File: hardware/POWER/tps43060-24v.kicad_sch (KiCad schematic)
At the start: 18 parts, among them Q1 CSD17313Q2, Q2 CSD17313Q2, U3 TPS43060RTE

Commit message: 硬件版本v2，待验证
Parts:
- C3, C5: footprint Resistor_SMD:R_0402_1005Metric -> Capacitor_SMD:C_0402_1005Metric
- C4, C6, C7, C8: footprint Capacitor_SMD:C_0805_2012Metric -> Capacitor_SMD:C_0603_1608Metric
- R7: value 76.8K -> 78.7K
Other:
- note added: "F=730K"
- note removed: "F=748K"
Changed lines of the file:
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@@
 		)
 	)
-	(text "F=748K"
+	(text "F=730K"
 		(exclude_from_sim no)
 		(at 104.902 125.73 0)
@@
 			)
 		)
-		(property "Footprint" "Resistor_SMD:R_0402_1005Metric"
+		(property "Footprint" "Capacitor_SMD:C_0402_1005Metric"
 			(at 153.3652 107.95 0)
 			(effects
@@
 			)
 		)
-		(property "Footprint" "Resistor_SMD:R_0402_1005Metric"
+		(property "Footprint" "Capacitor_SMD:C_0402_1005Metric"
 			(at 153.3652 85.09 0)
 			(effects
@@
 			)
 		)
-		(property "Footprint" "Capacitor_SMD:C_0805_2012Metric"
+		(property "Footprint" "Capacitor_SMD:C_0603_1608Metric"
 			(at 61.9252 101.6 0)
 			(effects
@@
 			)
 		)
-		(property "Footprint" "Capacitor_SMD:C_0805_2012Metric"
+		(property "Footprint" "Capacitor_SMD:C_0603_1608Metric"
 			(at 228.2952 110.49 0)
 			(effects
@@
 			)
 		)
-		(property "Footprint" "Capacitor_SMD:C_0805_2012Metric"
+		(property "Footprint" "Capacitor_SMD:C_0603_1608Metric"
 			(at 210.5152 110.49 0)
 			(effects
@@
 			)
 		)
-		(property "Value" "76.8K"
+		(property "Value" "78.7K"
 			(at 101.6 121.9199 0)
 			(effects
@@
 			)
 		)
-		(property "Footprint" "Capacitor_SMD:C_0805_2012Metric"
+		(property "Footprint" "Capacitor_SMD:C_0603_1608Metric"
 			(at 219.4052 110.49 0)
 			(effects

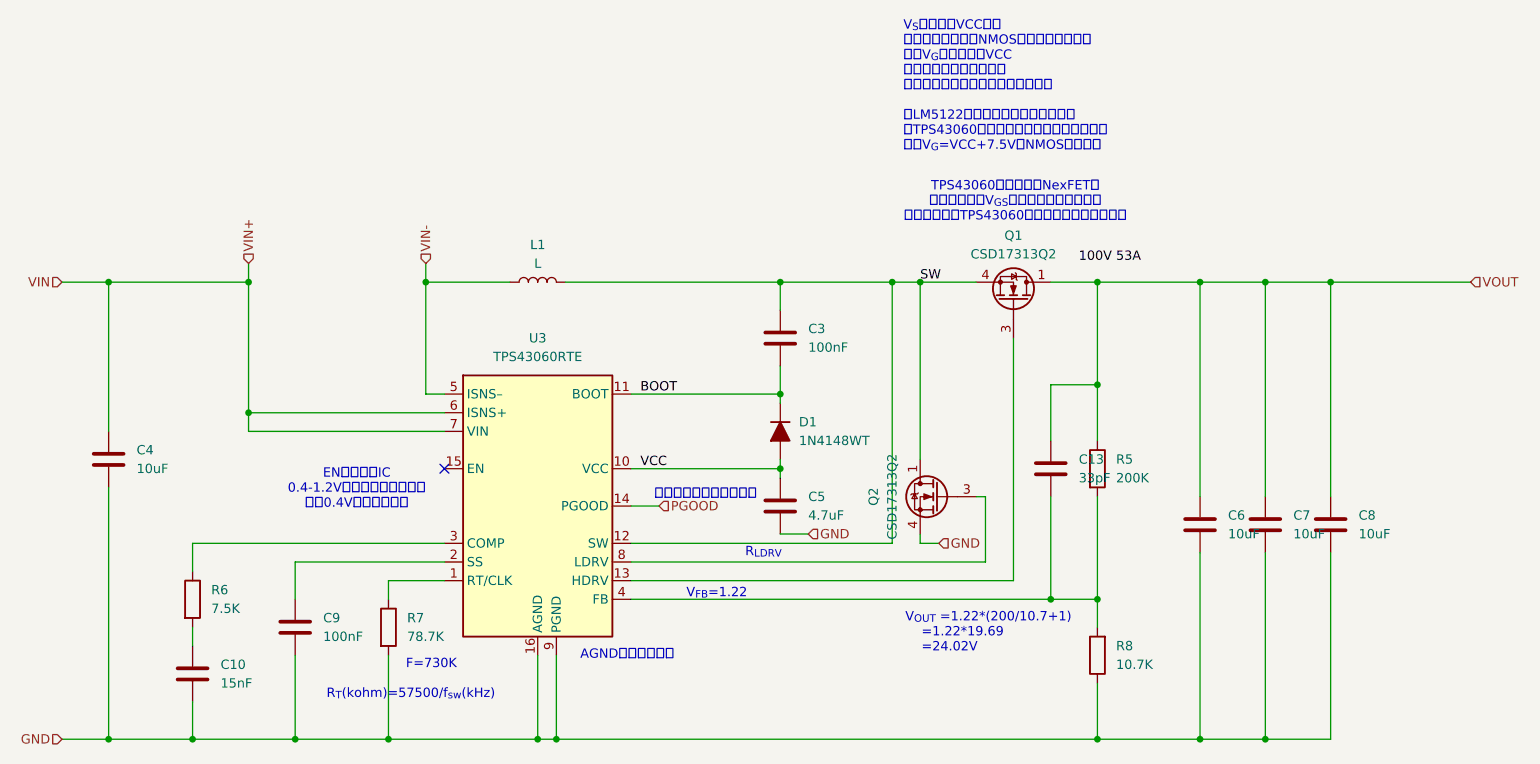
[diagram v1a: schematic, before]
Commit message: lis2dw12由于错误配置了cs脚，导致进入了spi模式，但电路设计上为iic的连接方式，无法读取方向，现在已经修正，但是代码设置成了固定方向。同步升压整流确实降低了不少发热，但是好像添加的ldo由于oled电流较大，带来的额外热量更多，之后可能还是考虑使用dcdc降压
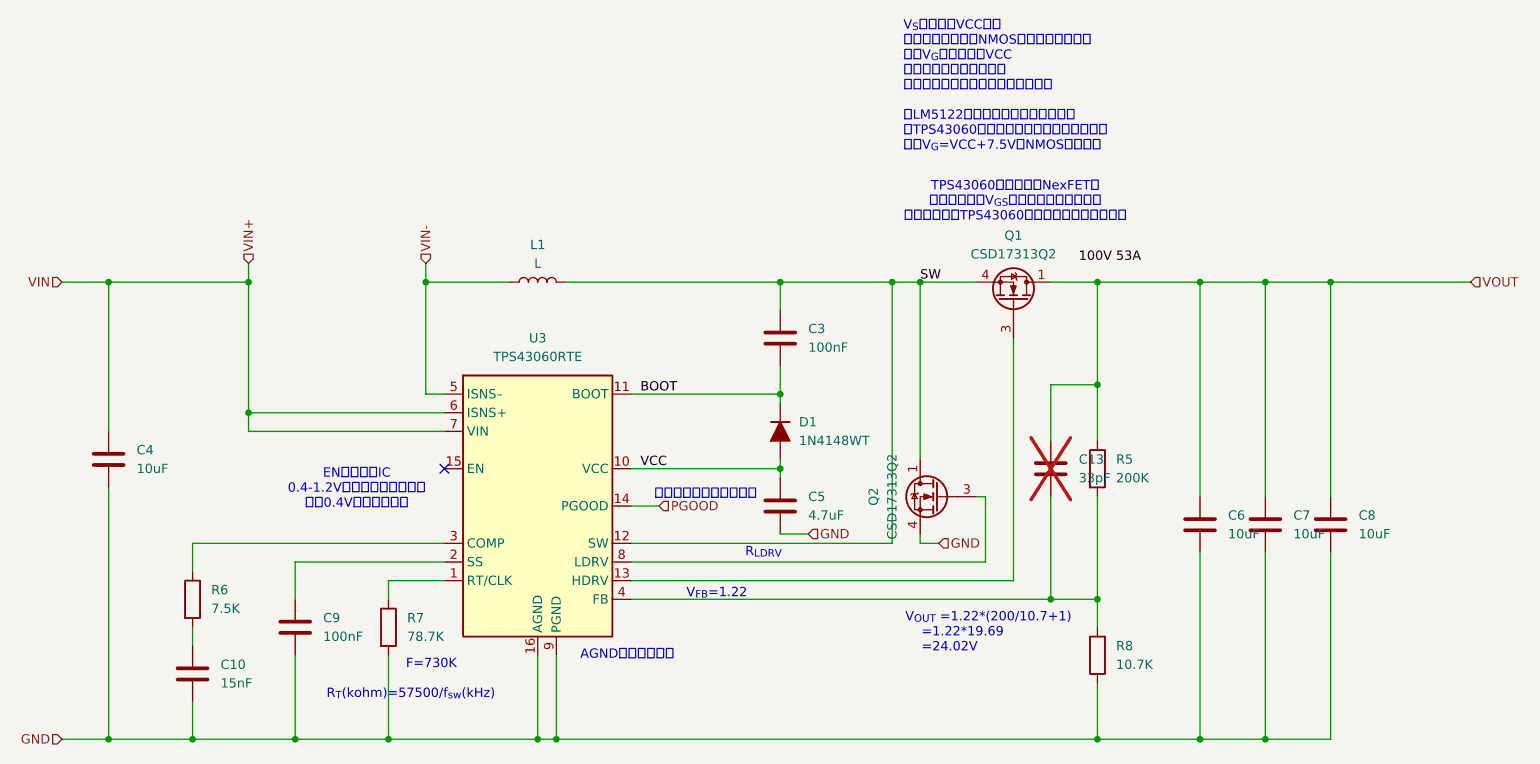
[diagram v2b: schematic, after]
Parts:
- C13: now not fitted; now left out of the parts list
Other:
- note added: "V_{S}电平即为VCC电平 所以替代二极管的NMOS如果需要导通的话 需要V_{G}的电平大于VCC 正常情况下不容易得到， 需要用能够抬升电压的电路进行驱动 在LM5122中，使用了电荷泵抬高电压 在TPS43060中使用了某种偏置方法抬高电压 使得V_{G}=VCC+7.5V，NMOS能够导通"
- note removed: "V_{S}电平即为VCC电平 所以替代二极管的NMOS如果需要导通的话 需要V_{G}的电平大于VCC 正常情况下不容易得到， 需要用能够抬升电压的电路进行驱动 在LM5122中，使用了电荷泵抬高电压 在TPS43060中使用了某种偏置方法太高电压 使得V_{G}=VCC+7.5V，NMOS能够导通"
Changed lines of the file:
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@@
 (kicad_sch
-	(version 20231120)
+	(version 20250114)
 	(generator "eeschema")
-	(generator_version "8.0")
+	(generator_version "9.0")
 	(paper "A4")
+	(text "V_{S}电平即为VCC电平\n所以替代二极管的NMOS如果需要导通的话\n需要V_{G}的电平大于VCC\n正常情况下不容易得到，\n需要用能够抬升电压的电路进行驱动\n\n在LM5122中，使用了电荷泵抬高电压\n在TPS43060中使用了某种偏置方法抬高电压\n使得V_{G}=VCC+7.5V，NMOS能够导通"
+		(exclude_from_sim no)
+		(at 169.164 46.99 0)
+		(effects
+			(font
+				(size 1.27 1.27)
+			)
+			(justify left)
+		)
+	)
+	(text "EN浮空使能IC\n0.4-1.2V进入低电流备用模式\n低于0.4V进入关断模式"
+		(exclude_from_sim no)
+		(at 94.742 101.854 0)
+		(effects
+			(font
+				(size 1.27 1.27)
+			)
+		)
+	)
+	(text "V_{FB}=1.22"
+		(exclude_from_sim no)
+		(at 143.764 116.078 0)
+		(effects
+			(font
+				(size 1.27 1.27)
+			)
+		)
+	)
+	(text "V_{OUT} =1.22*(200/10.7+1)\n	=1.22*19.69\n	=24.02V"
+		(exclude_from_sim no)
+		(at 169.418 121.412 0)
+		(effects
+			(font
+				(size 1.27 1.27)
+			)
+			(justify left)
+		)
+	)
+	(text "AGND注意单点接地"
+		(exclude_from_sim no)
+		(at 131.572 124.46 0)
+		(effects
+			(font
+				(size 1.27 1.27)
+			)
+		)
+	)
+	(text "开漏输出，需要上拉电阻"
+		(exclude_from_sim no)
+		(at 142.24 102.616 0)
+		(effects
+			(font
+				(size 1.27 1.27)
+			)
+		)
+	)
+	(text "TPS43060也可以使用NexFET，\n同时，更高的V_{GS}可以使导通电阻更低，\n但是相对的，TPS43060相对就会消耗更多的功耗"
+		(exclude_from_sim no)
+		(at 184.404 62.738 0)
+		(effects
+			(font
+				(size 1.27 1.27)
+			)
+		)
+	)
+	(text "F=730K"
+		(exclude_from_sim no)
+		(at 104.902 125.73 0)
+		(effects
+			(font
+				(size 1.27 1.27)
+			)
+		)
+	)
+	(text "R_{T}(kohm)=57500/f_{sw}(kHz)"
+		(exclude_from_sim no)
+		(at 102.108 129.794 0)
+		(effects
+			(font
+				(size 1.27 1.27)
+			)
+		)
+	)
+	(text "R_{LDRV}"
+		(exclude_from_sim no)
+		(at 150.114 110.49 0)
+		(effects
+			(font
+				(size 1.27 1.27)
+			)
+		)
+	)
 	(junction
 		(at 189.23 116.84)
@@
 		)
 	)
-	(text "V_{S}电平即为VCC电平\n所以替代二极管的NMOS如果需要导通的话\n需要V_{G}的电平大于VCC\n正常情况下不容易得到，\n需要用能够抬升电压的电路进行驱动\n\n在LM5122中，使用了电荷泵抬高电压\n在TPS43060中使用了某种偏置方法太高电压\n使得V_{G}=VCC+7.5V，NMOS能够导通"
-		(exclude_from_sim no)
-		(at 169.164 46.99 0)
-		(effects
-			(font
-				(size 1.27 1.27)
-			)
-			(justify left)
-		)
-	)
-	(text "EN浮空使能IC\n0.4-1.2V进入低电流备用模式\n低于0.4V进入关断模式"
-		(exclude_from_sim no)
-		(at 94.742 101.854 0)
-		(effects
-			(font
-				(size 1.27 1.27)
-			)
-		)
-	)
-	(text "V_{FB}=1.22"
-		(exclude_from_sim no)
-		(at 143.764 116.078 0)
-		(effects
-			(font
-				(size 1.27 1.27)
-			)
-		)
-	)
-	(text "V_{OUT} =1.22*(200/10.7+1)\n	=1.22*19.69\n	=24.02V"
-		(exclude_from_sim no)
-		(at 169.418 121.412 0)
-		(effects
-			(font
-				(size 1.27 1.27)
-			)
-			(justify left)
-		)
-	)
-	(text "AGND注意单点接地"
-		(exclude_from_sim no)
-		(at 131.572 124.46 0)
-		(effects
-			(font
-				(size 1.27 1.27)
-			)
-		)
-	)
-	(text "开漏输出，需要上拉电阻"
-		(exclude_from_sim no)
-		(at 142.24 102.616 0)
-		(effects
-			(font
-				(size 1.27 1.27)
-			)
-		)
-	)
-	(text "TPS43060也可以使用NexFET，\n同时，更高的V_{GS}可以使导通电阻更低，\n但是相对的，TPS43060相对就会消耗更多的功耗"
-		(exclude_from_sim no)
-		(at 184.404 62.738 0)
-		(effects
-			(font
-				(size 1.27 1.27)
-			)
-		)
-	)
-	(text "F=730K"
-		(exclude_from_sim no)
-		(at 104.902 125.73 0)
-		(effects
-			(font
-				(size 1.27 1.27)
-			)
-		)
-	)
-	(text "R_{T}(kohm)=57500/f_{sw}(kHz)"
-		(exclude_from_sim no)
-		(at 102.108 129.794 0)
-		(effects
-			(font
-				(size 1.27 1.27)
-			)
-		)
-	)
-	(text "R_{LDRV}"
-		(exclude_from_sim no)
-		(at 150.114 110.49 0)
-		(effects
-			(font
-				(size 1.27 1.27)
-			)
-		)
-	)
 	(label "SW"
 		(at 171.45 73.66 0)
-		(fields_autoplaced yes)
 		(effects
 			(font
@@
 	(label "100V 53A"
 		(at 193.04 71.12 0)
-		(fields_autoplaced yes)
 		(effects
 			(font
@@
 	(label "BOOT"
 		(at 133.35 88.9 0)
-		(fields_autoplaced yes)
 		(effects
 			(font
@@
 	(label "VCC"
 		(at 133.35 99.06 0)
-		(fields_autoplaced yes)
 		(effects
 			(font
@@
 		(shape input)
 		(at 104.14 71.12 90)
-		(fields_autoplaced yes)
 		(effects
 			(font
@@
 		(shape input)
 		(at 156.21 107.95 0)
-		(fields_autoplaced yes)
 		(effects
 			(font
@@
 		(shape input)
 		(at 246.38 73.66 0)
-		(fields_autoplaced yes)
 		(effects
 			(font
@@
 		(shape input)
 		(at 135.89 104.14 0)
-		(fields_autoplaced yes)
 		(effects
 			(font
@@
 		(shape input)
 		(at 54.61 73.66 180)
-		(fields_autoplaced yes)
 		(effects
 			(font
@@
 		(shape input)
 		(at 173.99 109.22 0)
-		(fields_autoplaced yes)
 		(effects
 			(font
@@
 		(shape input)
 		(at 54.61 135.89 180)
-		(fields_autoplaced yes)
 		(effects
 			(font
@@
 		(shape input)
 		(at 80.01 71.12 90)
-		(fields_autoplaced yes)
 		(effects
 			(font
@@
 		(unit 1)
 		(exclude_from_sim no)
-		(in_bom yes)
-		(on_board yes)
-		(dnp no)
+		(in_bom no)
+		(on_board no)
+		(dnp yes)
 		(fields_autoplaced yes)
 		(property "Reference" "C13"
